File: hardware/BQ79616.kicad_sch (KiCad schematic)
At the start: 9 parts, among them CN7 4x100nF, IC2 BQ79616PAPR

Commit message: sync
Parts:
- added C39: 10nF, Capacitor_SMD:C_0603_1608Metric, symbol Device:C_Small
- added C40, C42, C43, C44, C45: 1uF, Capacitor_SMD:C_0603_1608Metric, symbol Device:C_Small
- added C41: 100nF, Capacitor_SMD:C_0603_1608Metric, symbol Device:C_Small
- added C46, C47, C48, C49: 220pF, Capacitor_SMD:C_0603_1608Metric, symbol Device:C_Small
- added Q2: 100V/2W, Package_TO_SOT_SMD:SOT-223-3_TabPin2, symbol Device:Q_NPN_BCE
- added R53: 100, Resistor_SMD:R_0603_1608Metric, symbol PUTM_EV_BMS_HV_Slave_2021-rescue:R_Small-Device
- added R54: 200, Resistor_SMD:R_0603_1608Metric, symbol PUTM_EV_BMS_HV_Slave_2021-rescue:R_Small-Device
- added R55, R58: 1k, Resistor_SMD:R_0603_1608Metric, symbol PUTM_EV_BMS_HV_Slave_2021-rescue:R_Small-Device
- added R56, R57, R59, R60: 49, Resistor_SMD:R_0603_1608Metric, symbol PUTM_EV_BMS_HV_Slave_2021-rescue:R_Small-Device
- C38: value 10nF -> 10nF/100V
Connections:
- net C1-: now also C38.1, IC2.36 (REFHM), IC2.39 (AVSS), IC2.46 (CVSS), IC2.50 (DVSS), IC2.65 (EP), C39.2, C40.2, C41.2, C42.2, C43.2, C44.2, C45.2, C46.2, C47.2, C48.2, C49.2, R54.1
- net C16+: now also R52.1
- net C8+: now also IC2.63 (BBN)
- net C9+: now also IC2.64 (BBP)
- net CB11: no longer IC2.14 (CB10)
- net V-: no longer C38.1, IC2.65 (EP), R52.1
- net at IC2.37 (REFHP): now also C43.1
- net at IC2.38 (AVDD): now also C40.1
- net at IC2.40 (COMLP): now also C47.1, R58.2, R60.1
- net at IC2.41 (COMLN): now also C46.1, R58.1, R59.2
- net at IC2.42 (COMHN): now also C48.1, R55.1, R57.1
- net at IC2.43 (COMHP): now also C49.1, R55.2, R56.2
- net at IC2.44 (NEG5V): now also C41.1
- net at IC2.45 (CVDD): now also C45.1
- net at IC2.47 (LDOIN): now also Q2.3 (E)
- net at IC2.48 (NPNB): now also Q2.1 (B)
- net at IC2.49 (DVDD): now also C44.1
- net TSREF: now reaches IC2.51 (TSREF)
- net TSREF: now also C42.1
- net VREF2: no longer names the net of R2.2, RN7.5 (R4.2), RN7.6 (R3.2), RN7.7 (R2.2), RN7.8 (R1.2)
- new net: C39.1, Q2.2 (C), R53.2
- new net: R53.1, R54.2
- new net CB10: IC2.14 (CB10)
- new net COMHN: R57.2
- new net COMHP: R56.1
- new net COMLN: R59.1
- new net COMLP: R60.2
- no-connect marks 0 -> 3
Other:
- note added: "BQ79616"
- note removed: "CELL/TEMP DISCONN"
- note removed: "LTC"
- note removed: "sprawdzic jeszcze tego sipa"
- moved on the sheet: C38, C?, CN7, IC2, R2, R50, R51, R52, RN7

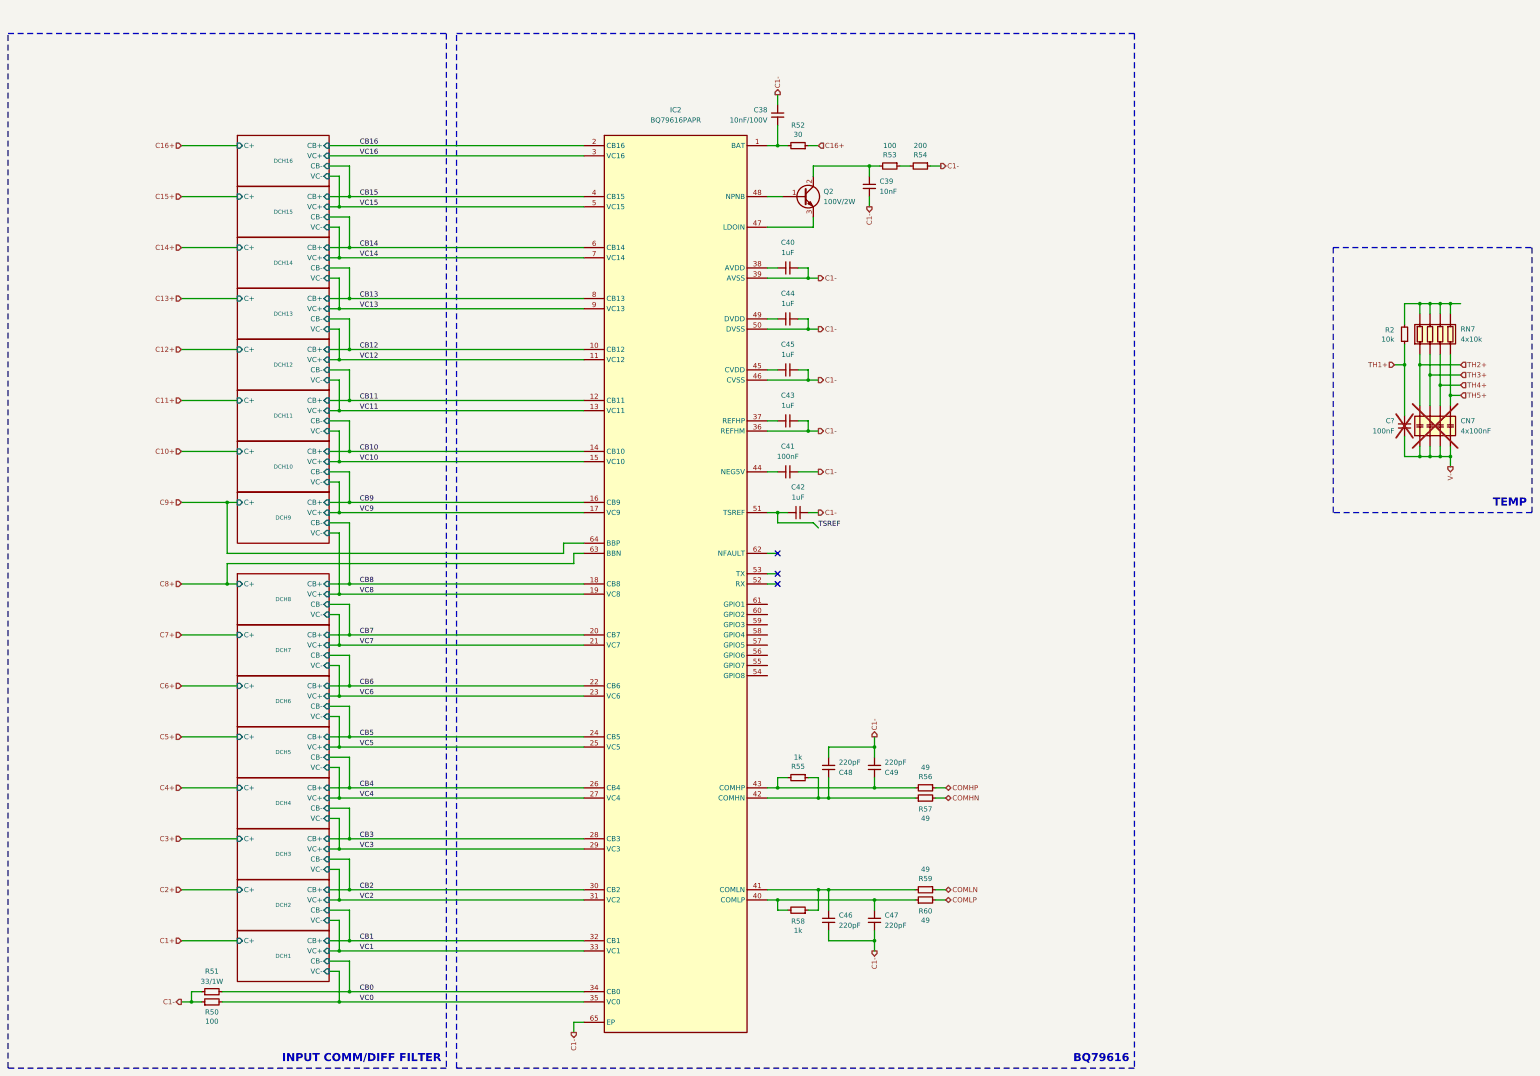
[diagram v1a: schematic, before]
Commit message: changed back harwin connectors, COM first fitting
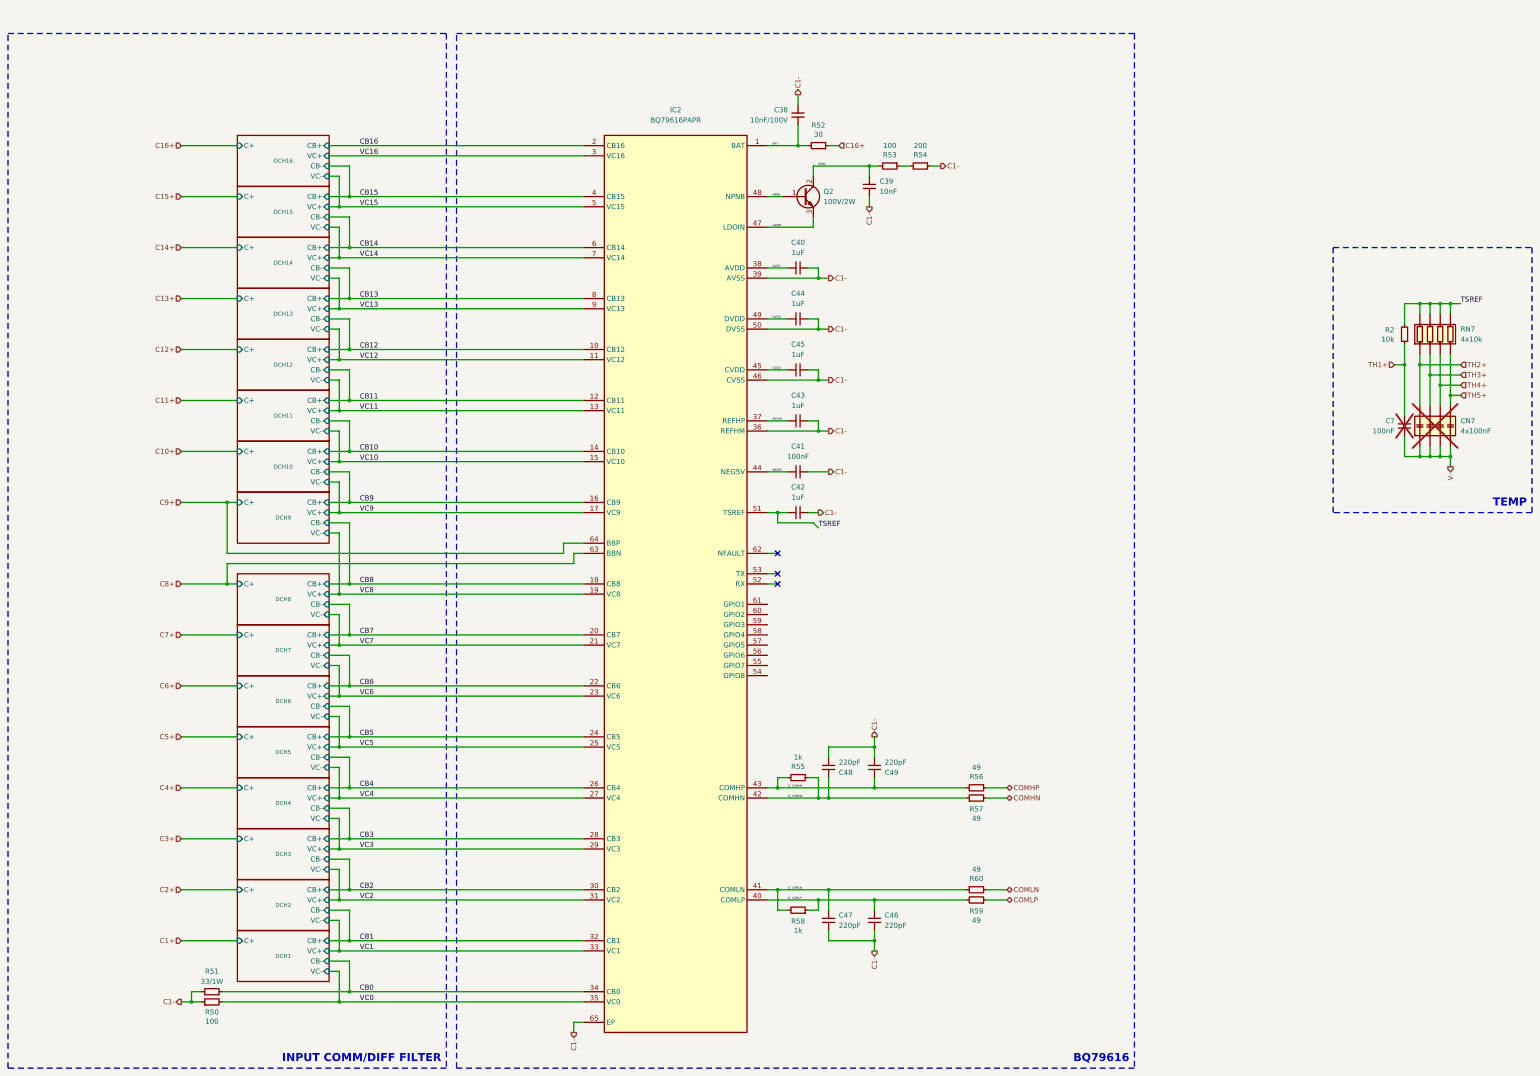
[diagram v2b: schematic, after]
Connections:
- net COMLN: now also R60.2; no longer R59.1
- net COMLP: now also R59.1; no longer R60.2
- net TSREF: now also R2.2, RN7.5 (R4.2), RN7.6 (R3.2), RN7.7 (R2.2), RN7.8 (R1.2)
- net IC_COMLP: now reaches C46.1, R58.1, R59.2
- net IC_COMLP: now also IC2.40 (COMLP); no longer IC2.41 (COMLN)
- net IC_COMHP: now reaches C49.1, IC2.43 (COMHP), R55.2, R56.2
- net CVDD: now reaches C45.1, IC2.45 (CVDD)
- net IC_COMLN: now reaches C47.1, R58.2, R60.1
- net IC_COMLN: now also IC2.41 (COMLN); no longer IC2.40 (COMLP)
- net IC_COMHN: now reaches C48.1, IC2.42 (COMHN), R55.1, R57.1
- net DVDD: now reaches C44.1, IC2.49 (DVDD)
- net BAT: now reaches C38.2, IC2.1 (BAT), R52.2
- net NPNB: now reaches IC2.48 (NPNB), Q2.1 (B)
- net NPNC: now reaches C39.1, Q2.2 (C), R53.2
- net LDOIN: now reaches IC2.47 (LDOIN), Q2.3 (E)
- net REFHM: now reaches C43.1, IC2.37 (REFHP)
- net AVDD: now reaches C40.1, IC2.38 (AVDD)
- net NEG5V: now reaches C41.1, IC2.44 (NEG5V)
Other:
- moved on the sheet: C38, C40, C41, C43, C44, C45, C46, C47, R52, R56, R57, R59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

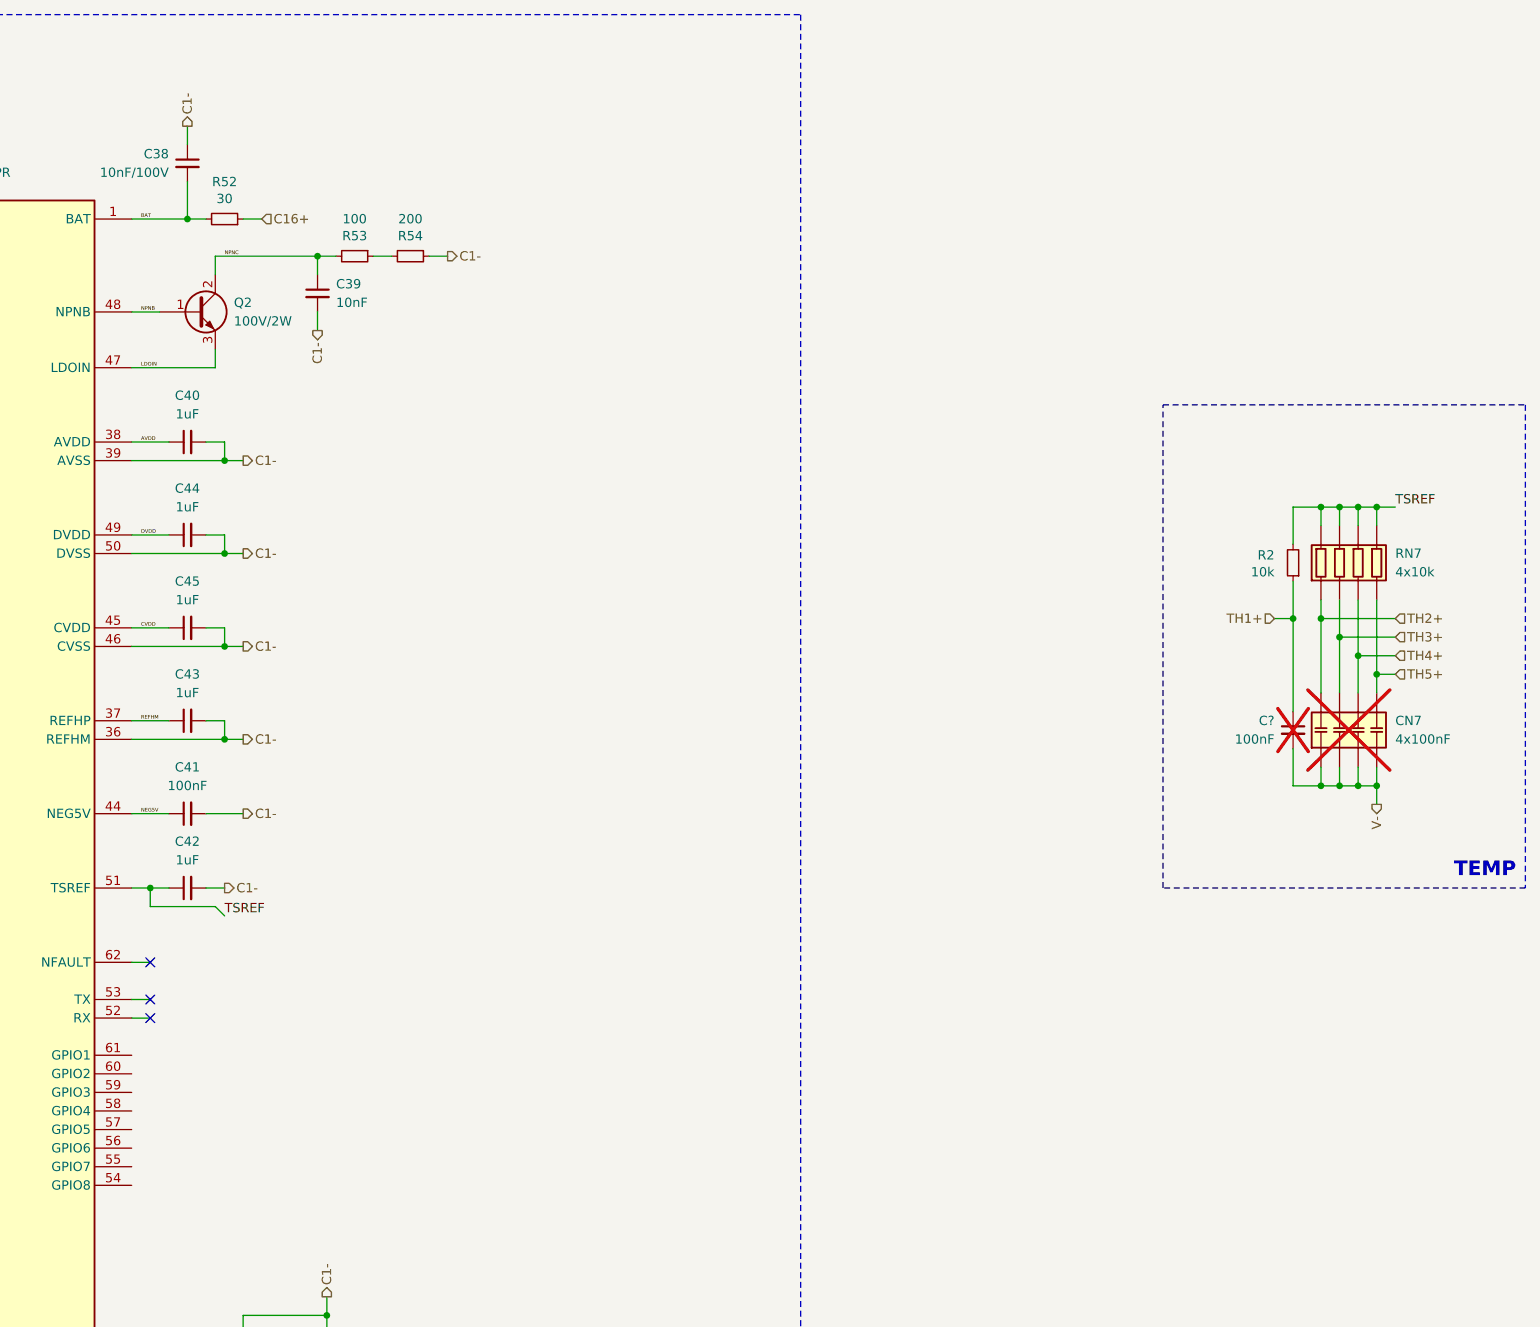
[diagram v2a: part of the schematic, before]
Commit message: some visual touch ups, added aux diodes for checking comm with IC, temp meas section, fliped the connector to the other side etc.
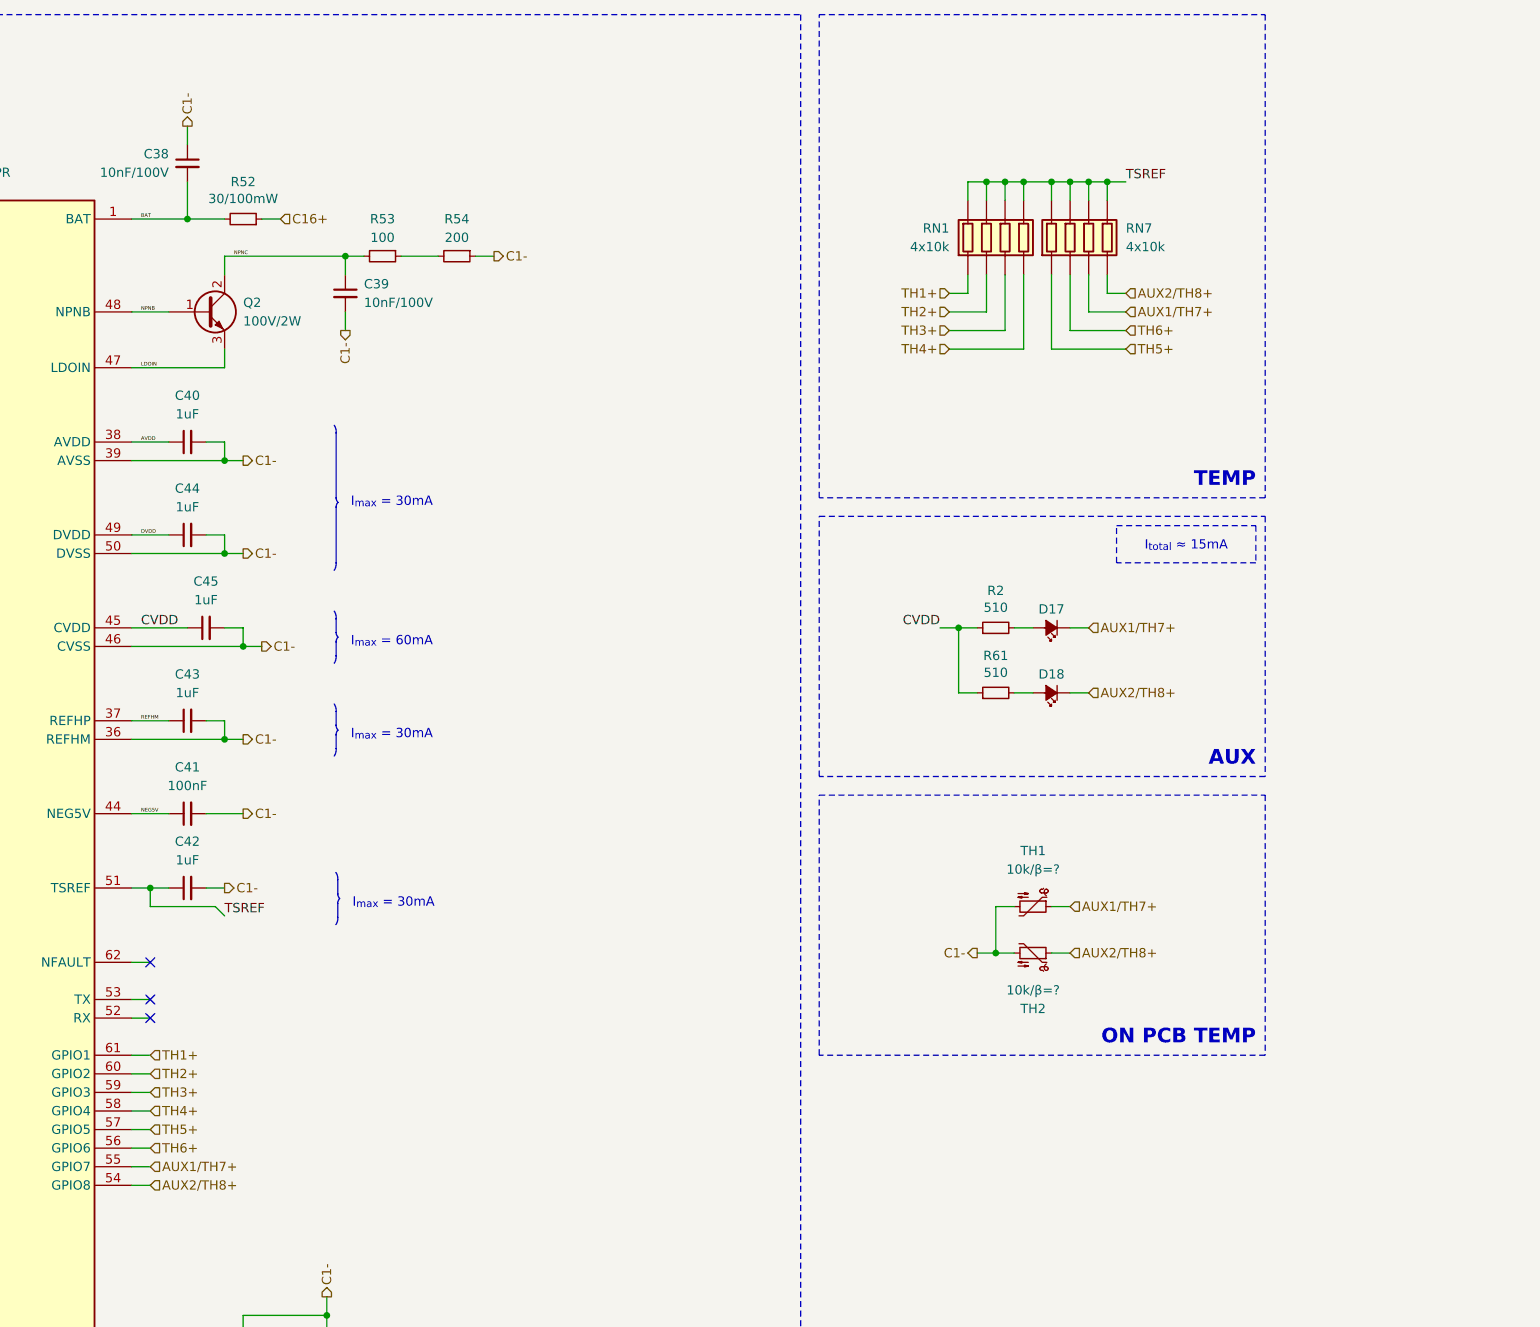
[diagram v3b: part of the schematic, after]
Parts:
- removed C?: 100nF, Capacitor_SMD:C_0603_1608Metric, symbol PUTM_EV_BMS_HV_Slave_2021-rescue:C_Small-Device
- removed CN7: 4x100nF, Resistor_SMD:R_Array_Convex_4x0603, symbol ca064x104k4racauto:CA064X104K4RACAUTO
- added D17, D18: LED, LED_SMD:LED_0603_1608Metric, symbol PUTM_EV_BMS_HV_Slave_2021-rescue:LED_Small_ALT-Device
- added R61: 510, Resistor_SMD:R_0603_1608Metric, symbol PUTM_EV_BMS_HV_Slave_2021-rescue:R_Small-Device
- added RN1: 4x10k, Resistor_SMD:R_Array_Convex_4x0603, symbol exb-v8v101jv:EXB-V8V101JV
- added TH1, TH2: 10k/β=?, Resistor_SMD:R_0603_1608Metric, symbol Device:Thermistor_NTC
- C39: value 10nF -> 10nF/100V
- R2: value 10k -> 510; Manufacturer_Part_Number -- -> RT0603FRE07330RL; Mouser Part Number (none) -> 603-RT0603FRE07330RL; Mouser Price/Stock (none) -> https://www.mouser.pl/ProductDetail/YAGEO/RT0603FRE07330RL?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
- R52: value 30 -> 30/100mW
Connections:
- net C1-: now also TH1.2, TH2.2
- net CVDD: now also R2.1, R61.1
- net TH1+: now also IC2.61 (GPIO1), RN1.1 (R1.1); no longer R2.1
- net TH2+: now also IC2.60 (GPIO2), RN1.2 (R2.1); no longer RN7.1 (R1.1)
- net TH3+: now also IC2.59 (GPIO3), RN1.3 (R3.1); no longer RN7.2 (R2.1)
- net TH4+: now also IC2.58 (GPIO4), RN1.4 (R4.1); no longer RN7.3 (R3.1)
- net TH5+: now also IC2.57 (GPIO5), RN7.1 (R1.1); no longer RN7.4 (R4.1)
- net TSREF: now also RN1.5 (R4.2), RN1.6 (R3.2), RN1.7 (R2.2), RN1.8 (R1.2); no longer R2.2
- net AUX2/TH8+: now reaches IC2.54 (GPIO8)
- net AUX2/TH8+: now also RN7.4 (R4.1), D18.1 (K), TH2.1
- net AUX1/TH7+: now reaches IC2.55 (GPIO7)
- net AUX1/TH7+: now also RN7.3 (R3.1), D17.1 (K), TH1.1
- net TH6+: now reaches IC2.56 (GPIO6)
- net TH6+: now also RN7.2 (R2.1)
- new net: D17.2 (A), R2.2
- new net: D18.2 (A), R61.2
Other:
- note added: "AUX"
- note added: "I_{max} = 30mA"
- note added: "I_{max} = 60mA"
- note added: "ON PCB TEMP"
- moved on the sheet: C39, C45, Q2, R52, R53, R54, RN7

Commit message: pcb layout 99.9% done - all sections named and placed also some initial routing
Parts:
- removed C46, C47, C48, C49: 220pF, Capacitor_SMD:C_0603_1608Metric, symbol Device:C_Small
- removed R55, R58: 1k, Resistor_SMD:R_0603_1608Metric, symbol PUTM_EV_BMS_HV_Slave_2021-rescue:R_Small-Device
- removed R56, R57, R59, R60: 49, Resistor_SMD:R_0603_1608Metric, symbol PUTM_EV_BMS_HV_Slave_2021-rescue:R_Small-Device
- removed RN1, RN7: 4x10k, Resistor_SMD:R_Array_Convex_4x0603, symbol exb-v8v101jv:EXB-V8V101JV
- added C4: 100nF, Capacitor_SMD:C_0603_1608Metric, symbol Device:C_Small
- added R62, R63, R64, R65, R66, R67, R68, R69: 10k, Resistor_SMD:R_0603_1608Metric, symbol PUTM_EV_BMS_HV_Slave_2021-rescue:R_Small-Device
- C39: value 10nF/100V -> 220nF/100V; footprint Capacitor_SMD:C_0603_1608Metric -> Capacitor_SMD:C_0805_2012Metric
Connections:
- net IC_COMHN is gone; now on net COMHN: IC2.42 (COMHN)
- net IC_COMHP is gone; now on net COMHP: IC2.43 (COMHP)
- net IC_COMLN is gone; now on net COMLN: IC2.41 (COMLN)
- net IC_COMLP is gone; now on net COMLP: IC2.40 (COMLP)
- net AUX1/TH7+: now also R68.1
- net AUX2/TH8+: now also R69.1
- net C1-: no longer C39.2, C40.2, C41.2, C42.2, C43.2, C44.2, C45.2, IC2.36 (REFHM), IC2.39 (AVSS), IC2.46 (CVSS), IC2.50 (DVSS), IC2.65 (EP), R50.1, R51.1, R54.1, TH1.2, TH2.2
- net C16+: now also R54.1
- net C8+: no longer IC2.63 (BBN)
- net C9+: no longer IC2.64 (BBP)
- net LDOIN: now also C4.1
- net TH1+: now also R62.1
- net TH2+: now also R63.1
- net TH3+: now also R64.1
- net TH4+: now also R65.1
- net TH5+: now also R66.1
- net TH6+: now also R67.1
- net TSREF: now also R62.2, R63.2, R64.2, R65.2, R66.2, R67.2, R68.2, R69.2
- new net GND: C39.2, C4.2, C40.2, C41.2, C42.2, C43.2, C44.2, C45.2, IC2.36 (REFHM), IC2.39 (AVSS), IC2.46 (CVSS), IC2.50 (DVSS), IC2.65 (EP), R50.1, R51.1, TH1.2, TH2.2
- no-connect marks 3 -> 5
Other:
- moved on the sheet: C39, D17, D18, R2, R53, R54, R61, TH1, TH2
